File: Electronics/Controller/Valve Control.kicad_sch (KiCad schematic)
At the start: 2 parts, among them J20 FRONT HEIGHT, J21 REAR HEIGHT

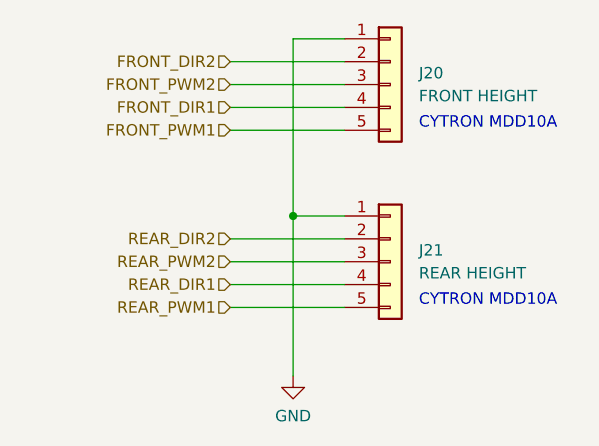
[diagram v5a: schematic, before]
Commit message: Renamed valve control connectors and reordered pins to match pinout of MDD10A connectors.
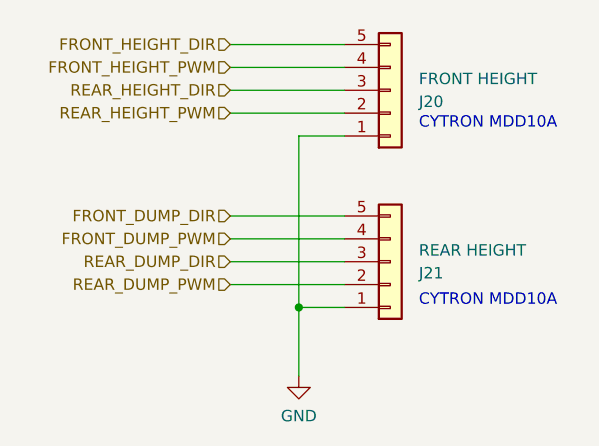
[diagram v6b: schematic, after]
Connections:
- net FRONT_DIR1 renamed FRONT_HEIGHT_PWM
- net FRONT_DIR2 renamed REAR_HEIGHT_PWM
- net FRONT_PWM1 renamed FRONT_HEIGHT_DIR
- net FRONT_PWM2 renamed REAR_HEIGHT_DIR
- net REAR_DIR1 renamed FRONT_DUMP_PWM
- net REAR_DIR2 renamed REAR_DUMP_PWM
- net REAR_PWM1 renamed FRONT_DUMP_DIR
- net REAR_PWM2 renamed REAR_DUMP_DIR
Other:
- moved on the sheet: J20
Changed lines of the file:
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@@
     (comment 2 "Provided as-is, no warranty express or implied. Use at your own risk")
   )
-  (junction (at 141.605 97.79) (diameter 0) (color 0 0 0 0)
+  (junction (at 142.24 107.95) (diameter 0) (color 0 0 0 0)
   )
-  (wire (pts (xy 134.62 80.645) (xy 147.32 80.645))
-    (stroke (width 0) (type default))
-  )
-  (wire (pts (xy 147.32 78.105) (xy 141.605 78.105))
+  (wire (pts (xy 142.24 107.95) (xy 142.24 115.57))
     (stroke (width 0) (type default))
   )
@@
     (stroke (width 0) (type default))
   )
-  (wire (pts (xy 141.605 97.79) (xy 147.32 97.79))
+  (wire (pts (xy 142.24 88.9) (xy 142.24 107.95))
     (stroke (width 0) (type default))
   )
-  (wire (pts (xy 141.605 78.105) (xy 141.605 97.79))
+  (wire (pts (xy 134.62 86.36) (xy 147.32 86.36))
     (stroke (width 0) (type default))
   )
-  (wire (pts (xy 134.62 100.33) (xy 147.32 100.33))
+  (wire (pts (xy 147.32 88.9) (xy 142.24 88.9))
+    (stroke (width 0) (type default))
+  )
+  (wire (pts (xy 134.62 78.74) (xy 147.32 78.74))
     (stroke (width 0) (type default))
   )
@@
     (stroke (width 0) (type default))
   )
-  (wire (pts (xy 134.62 83.185) (xy 147.32 83.185))
+  (wire (pts (xy 134.62 83.82) (xy 147.32 83.82))
     (stroke (width 0) (type default))
   )
-  (wire (pts (xy 134.62 107.95) (xy 147.32 107.95))
+  (wire (pts (xy 147.32 107.95) (xy 142.24 107.95))
     (stroke (width 0) (type default))
   )
-  (wire (pts (xy 134.62 88.265) (xy 147.32 88.265))
+  (wire (pts (xy 134.62 97.79) (xy 147.32 97.79))
     (stroke (width 0) (type default))
   )
-  (wire (pts (xy 134.62 85.725) (xy 147.32 85.725))
+  (wire (pts (xy 134.62 81.28) (xy 147.32 81.28))
     (stroke (width 0) (type default))
   )
-  (wire (pts (xy 141.605 97.79) (xy 141.605 115.57))
+  (wire (pts (xy 134.62 100.33) (xy 147.32 100.33))
     (stroke (width 0) (type default))
   )
@@
     (effects (font (size 1.27 1.27)) (justify left bottom))
   )
-  (hierarchical_label "REAR_PWM1" (shape input) (at 134.62 107.95 180) (fields_autoplaced)
+  (hierarchical_label "REAR_DUMP_PWM" (shape input) (at 134.62 105.41 180) (fields_autoplaced)
     (effects (font (size 1.27 1.27)) (justify right))
   )
-  (hierarchical_label "REAR_DIR1" (shape input) (at 134.62 105.41 180) (fields_autoplaced)
+  (hierarchical_label "REAR_DUMP_DIR" (shape input) (at 134.62 102.87 180) (fields_autoplaced)
     (effects (font (size 1.27 1.27)) (justify right))
   )
-  (hierarchical_label "FRONT_DIR2" (shape input) (at 134.62 80.645 180) (fields_autoplaced)
+  (hierarchical_label "REAR_HEIGHT_DIR" (shape input) (at 134.62 83.82 180) (fields_autoplaced)
     (effects (font (size 1.27 1.27)) (justify right))
   )
-  (hierarchical_label "FRONT_PWM1" (shape input) (at 134.62 88.265 180) (fields_autoplaced)
+  (hierarchical_label "FRONT_HEIGHT_PWM" (shape input) (at 134.62 81.28 180) (fields_autoplaced)
     (effects (font (size 1.27 1.27)) (justify right))
   )
-  (hierarchical_label "REAR_DIR2" (shape input) (at 134.62 100.33 180) (fields_autoplaced)
+  (hierarchical_label "FRONT_DUMP_DIR" (shape input) (at 134.62 97.79 180) (fields_autoplaced)
     (effects (font (size 1.27 1.27)) (justify right))
   )
-  (hierarchical_label "FRONT_PWM2" (shape input) (at 134.62 83.185 180) (fields_autoplaced)
+  (hierarchical_label "REAR_HEIGHT_PWM" (shape input) (at 134.62 86.36 180) (fields_autoplaced)
     (effects (font (size 1.27 1.27)) (justify right))
   )
-  (hierarchical_label "REAR_PWM2" (shape input) (at 134.62 102.87 180) (fields_autoplaced)
+  (hierarchical_label "FRONT_DUMP_PWM" (shape input) (at 134.62 100.33 180) (fields_autoplaced)
     (effects (font (size 1.27 1.27)) (justify right))
   )
-  (hierarchical_label "FRONT_DIR1" (shape input) (at 134.62 85.725 180) (fields_autoplaced)
+  (hierarchical_label "FRONT_HEIGHT_DIR" (shape input) (at 134.62 78.74 180) (fields_autoplaced)
     (effects (font (size 1.27 1.27)) (justify right))
   )
-  (symbol (lib_id "Connector_Generic:Conn_01x05") (at 152.4 83.185 0) (unit 1)
-    (in_bom yes) (on_board yes) (dnp no) (fields_autoplaced)
-    (property "Reference" "J20" (at 155.575 81.915 0)
+  (symbol (lib_id "Connector_Generic:Conn_01x05") (at 152.4 83.82 0) (mirror x) (unit 1)
+    (in_bom yes) (on_board yes) (dnp no)
+    (property "Reference" "J20" (at 155.575 85.09 0)
       (effects (font (size 1.27 1.27)) (justify left))
     )
-    (property "Value" "FRONT HEIGHT" (at 155.575 84.455 0)
+    (property "Value" "FRONT HEIGHT" (at 155.575 82.55 0)
       (effects (font (size 1.27 1.27)) (justify left))
     )
-    (property "Footprint" "Connector_JST:JST_PH_B5B-PH-K_1x05_P2.00mm_Vertical" (at 152.4 83.185 0)
+    (property "Footprint" "Connector_JST:JST_PH_B5B-PH-K_1x05_P2.00mm_Vertical" (at 152.4 83.82 0)
       (effects (font (size 1.27 1.27)) hide)
     )
-    (property "Datasheet" "~" (at 152.4 83.185 0)
+    (property "Datasheet" "~" (at 152.4 83.82 0)
       (effects (font (size 1.27 1.27)) hide)
     )
-    (property "manf#" "B5B-PH-K-S" (at 152.4 83.185 0)
+    (property "manf#" "B5B-PH-K-S" (at 152.4 83.82 0)
       (effects (font (size 1.27 1.27)) hide)
     )
-    (property "Field5" "" (at 152.4 83.185 0)
+    (property "Field5" "" (at 152.4 83.82 0)
       (effects (font (size 1.27 1.27)) hide)
     )
@@
     )
   )
-  (symbol (lib_id "power:GND") (at 141.605 115.57 0) (unit 1)
+  (symbol (lib_id "power:GND") (at 142.24 115.57 0) (unit 1)
     (in_bom yes) (on_board yes) (dnp no) (fields_autoplaced)
-    (property "Reference" "#PWR083" (at 141.605 121.92 0)
+    (property "Reference" "#PWR083" (at 142.24 121.92 0)
       (effects (font (size 1.27 1.27)) hide)
     )
-    (property "Value" "GND" (at 141.605 120.015 0)
+    (property "Value" "GND" (at 142.24 120.015 0)
       (effects (font (size 1.27 1.27)))
     )
-    (property "Footprint" "" (at 141.605 115.57 0)
+    (property "Footprint" "" (at 142.24 115.57 0)
       (effects (font (size 1.27 1.27)) hide)
     )
-    (property "Datasheet" "" (at 141.605 115.57 0)
+    (property "Datasheet" "" (at 142.24 115.57 0)
       (effects (font (size 1.27 1.27)) hide)
     )
@@
     )
   )
-  (symbol (lib_id "Connector_Generic:Conn_01x05") (at 152.4 102.87 0) (unit 1)
-    (in_bom yes) (on_board yes) (dnp no) (fields_autoplaced)
-    (property "Reference" "J21" (at 155.575 101.6 0)
+  (symbol (lib_id "Connector_Generic:Conn_01x05") (at 152.4 102.87 0) (mirror x) (unit 1)
+    (in_bom yes) (on_board yes) (dnp no)
+    (property "Reference" "J21" (at 155.575 104.14 0)
       (effects (font (size 1.27 1.27)) (justify left))
     )
-    (property "Value" "REAR HEIGHT" (at 155.575 104.14 0)
+    (property "Value" "REAR HEIGHT" (at 155.575 101.6 0)
       (effects (font (size 1.27 1.27)) (justify left))
     )

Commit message: Added 4.7uF caps to FT232RL on controller.
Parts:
- J20, J21: LCSC (none) -> C157993
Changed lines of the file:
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@@
   (title_block
     (title "Tandem Leveller Controller")
-    (date "2025-02-22")
+    (date "2025-03-11")
     (rev "V1.0")
     (company "(C) andy@britishideas.com 2025")
@@
       (effects (font (size 1.27 1.27)) hide)
     )
-    (property "Field5" "" (at 152.4 83.82 0)
+    (property "LCSC" "C157993" (at 152.4 83.82 0)
       (effects (font (size 1.27 1.27)) hide)
     )
@@
       (effects (font (size 1.27 1.27)) hide)
     )
+    (property "LCSC" "C157993" (at 152.4 102.87 0)
+      (effects (font (size 1.27 1.27)) hide)
+    )
